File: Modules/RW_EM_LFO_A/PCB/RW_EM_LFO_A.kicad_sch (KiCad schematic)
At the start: 20 parts, among them J1 IDC_02x05, J2 PJ301M-12, SW1 SW_SPDT, U1 TL072

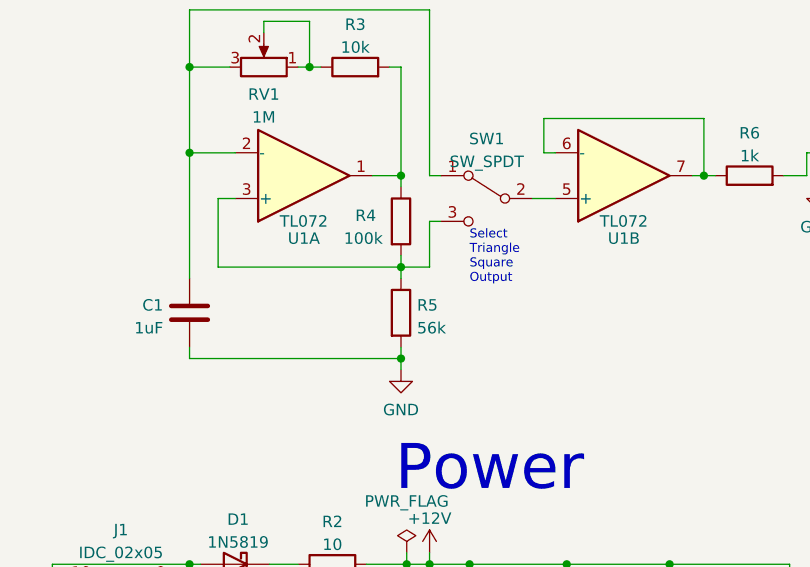
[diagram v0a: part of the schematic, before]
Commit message: Updated all schematics with link to repo. Also updated all readme files
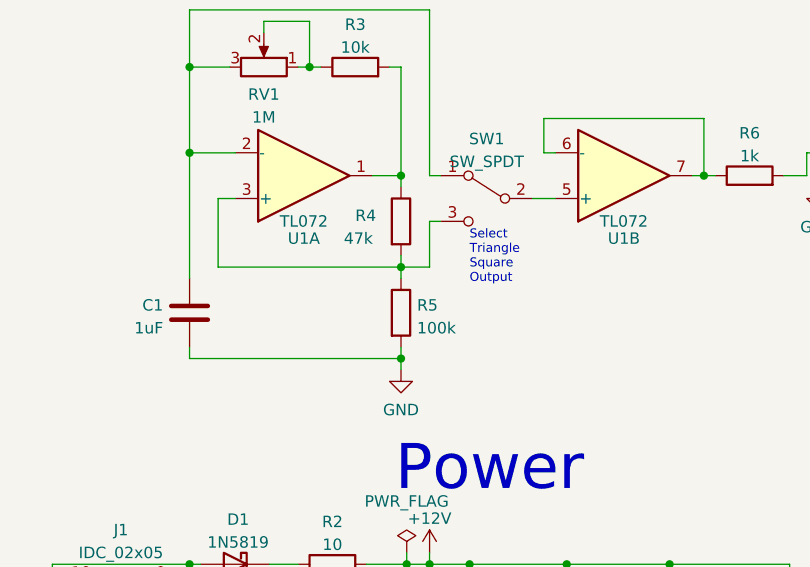
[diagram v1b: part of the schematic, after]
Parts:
- R4: value 100k -> 47k
- R5: value 56k -> 100k
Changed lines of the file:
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@@
   (title_block
     (title "RW_EM_LFO_A")
-    (date "2022-10-19")
-    (rev "2022-10-19")
+    (date "2022-10-22")
+    (rev "2022-10-22")
     (comment 1 "Licensed under CERN-OHL-S v2+")
+    (comment 2 "https://github.com/sunfl0w/RW_EM")
   )
   (junction (at 153.67 152.4) (diameter 0) (color 0 0 0 0)
@@
       (effects (font (size 1.27 1.27)) (justify left))
     )
-    (property "Value" "100k" (id 1) (at 117.475 97.155 0)
+    (property "Value" "47k" (id 1) (at 117.475 97.155 0)
       (effects (font (size 1.27 1.27)) (justify left))
     )
@@
       (effects (font (size 1.27 1.27)) (justify left))
     )
-    (property "Value" "56k" (id 1) (at 125.603 107.1122 0)
+    (property "Value" "100k" (id 1) (at 125.603 107.1122 0)
       (effects (font (size 1.27 1.27)) (justify left))
     )
@@
     )
     (path "/9dce71bd-2081-481d-928c-d53bac9e732f"
-      (reference "R4") (unit 1) (value "100k") (footprint "Resistor_THT:R_Axial_DIN0207_L6.3mm_D2.5mm_P10.16mm_Horizontal")
+      (reference "R4") (unit 1) (value "47k") (footprint "Resistor_THT:R_Axial_DIN0207_L6.3mm_D2.5mm_P10.16mm_Horizontal")
     )
     (path "/f08ecf7d-7367-4623-9b33-c90960f7cd3c"
-      (reference "R5") (unit 1) (value "56k") (footprint "Resistor_THT:R_Axial_DIN0207_L6.3mm_D2.5mm_P10.16mm_Horizontal")
+      (reference "R5") (unit 1) (value "100k") (footprint "Resistor_THT:R_Axial_DIN0207_L6.3mm_D2.5mm_P10.16mm_Horizontal")
     )
     (path "/ab6bc481-ee12-4f72-96d5-7e1d2704fc3d"
